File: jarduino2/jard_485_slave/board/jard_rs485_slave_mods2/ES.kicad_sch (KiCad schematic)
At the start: 29 parts, among them U1 BPC_Mod485

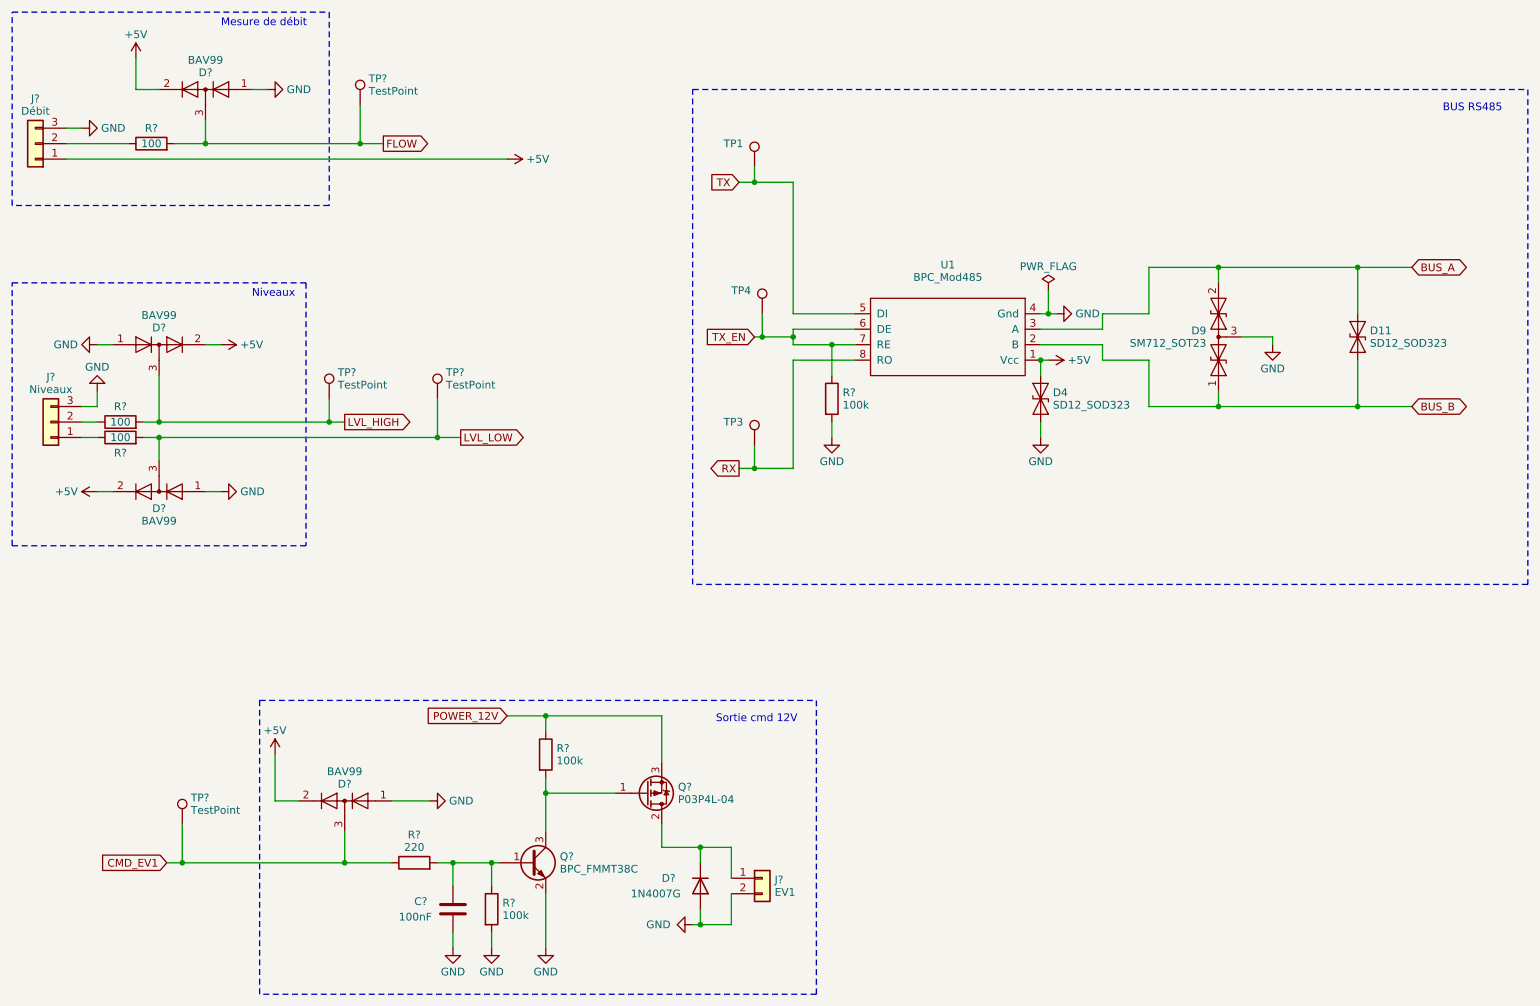
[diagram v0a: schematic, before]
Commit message: Suppression du module RS485 et remplacement par le CI MAX485E lui-même. Preparation version G...
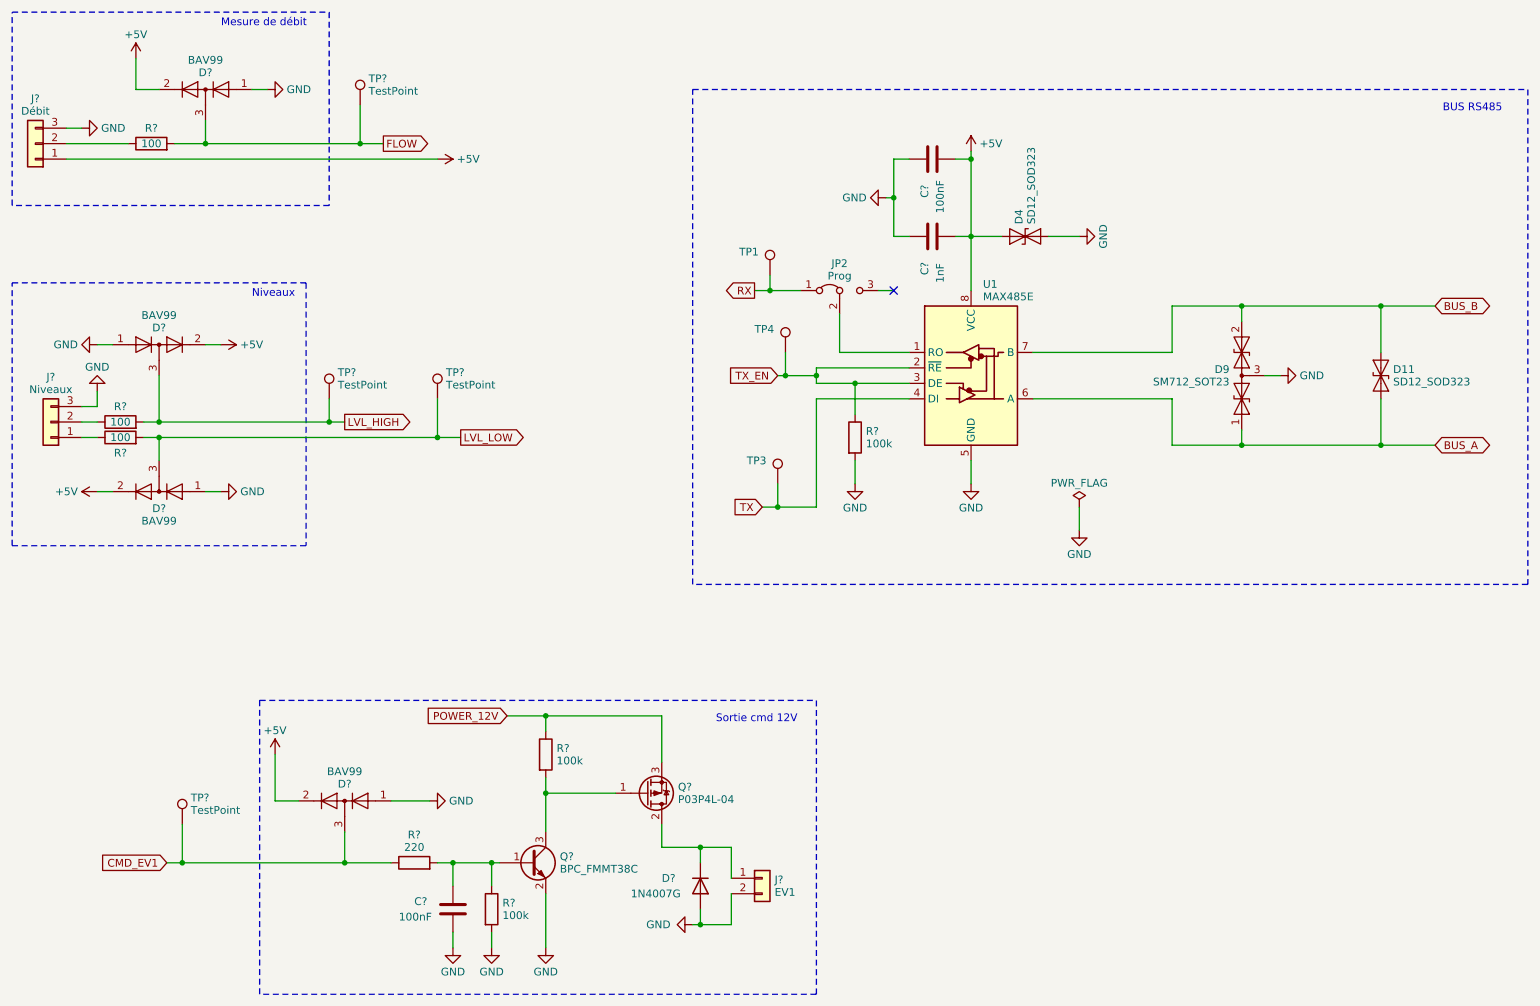
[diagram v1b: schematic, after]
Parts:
- removed U1: BPC_Mod485, bpc:BPC_Mod485, symbol bpc:BPC_Mod485
- added C?: 100nF, Capacitor_SMD:C_0603_1608Metric, symbol Device:C
- added C?: 1nF, Capacitor_SMD:C_0603_1608Metric, symbol Device:C
- added JP2: Prog, Connector_PinHeader_2.54mm:PinHeader_1x03_P2.54mm_Vertical, symbol Jumper:Jumper_3_Bridged12
- added U1: MAX485E, bpc:BPC_MAX485E_SOIC127P600X175-8N, symbol bpc:BPC_MAX485E
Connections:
- net +5V: now also C?.2, C?.2, U1.8 (VCC)
- net BUS_A: now also D11.1 (A1), D9.1 (A1), U1.6 (A); no longer D11.2 (A2), D9.2 (A2)
- net BUS_B: now also D11.2 (A2), D9.2 (A2), U1.7 (B); no longer D11.1 (A1), D9.1 (A1)
- net GND: now also C?.1, C?.1, U1.5 (GND)
- net RX: now also TP1.1, JP2.1 (A); no longer TP3.1
- net TX: now also TP3.1, U1.4 (DI); no longer TP1.1
- net TX_EN: now also U1.2 (~{RE}), U1.3 (DE)
- new net: JP2.2 (C), U1.1 (RO)
- no-connect marks 0 -> 1
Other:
- moved on the sheet: D11, D4, D9, R?, TP1, TP3, TP4

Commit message: Finitions avant production
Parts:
- added TP1 (x2): TestPoint, TestPoint:TestPoint_Pad_D1.5mm, symbol Connector:TestPoint
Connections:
- net BUS_A: now also TP1.1
- net BUS_B: now also TP1.1
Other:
- moved on the sheet: D11
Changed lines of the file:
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@@
   (junction (at 107.95 137.16) (diameter 0) (color 0 0 0 0)
   )
+  (junction (at 251.46 69.85) (diameter 0) (color 0 0 0 0)
+  )
   (junction (at 146.05 102.87) (diameter 0) (color 0 0 0 0)
+  )
+  (junction (at 251.46 92.71) (diameter 0) (color 0 0 0 0)
   )
   (junction (at 90.17 91.44) (diameter 0) (color 0 0 0 0)
@@
     (stroke (width 0) (type default))
   )
+  (wire (pts (xy 251.46 69.85) (xy 254 69.85))
+    (stroke (width 0) (type default))
+  )
   (wire (pts (xy 77.47 43.18) (xy 81.28 43.18))
     (stroke (width 0) (type default))
@@
     (stroke (width 0) (type default))
   )
-  (wire (pts (xy 245.11 85.09) (xy 245.11 92.71))
+  (wire (pts (xy 251.46 92.71) (xy 254 92.71))
+    (stroke (width 0) (type default))
+  )
+  (wire (pts (xy 245.11 83.82) (xy 245.11 92.71))
     (stroke (width 0) (type default))
   )
@@
     (stroke (width 0) (type default))
   )
-  (wire (pts (xy 245.11 92.71) (xy 254 92.71))
+  (wire (pts (xy 245.11 92.71) (xy 251.46 92.71))
     (stroke (width 0) (type default))
   )
@@
     (stroke (width 0) (type default))
   )
-  (wire (pts (xy 245.11 69.85) (xy 245.11 77.47))
+  (wire (pts (xy 245.11 69.85) (xy 245.11 76.2))
     (stroke (width 0) (type default))
   )
@@
     (stroke (width 0) (type default))
   )
+  (wire (pts (xy 251.46 68.58) (xy 251.46 69.85))
+    (stroke (width 0) (type default))
+  )
   (wire (pts (xy 74.93 156.21) (xy 74.93 161.29))
     (stroke (width 0) (type default))
@@
     (stroke (width 0) (type default))
   )
-  (wire (pts (xy 245.11 69.85) (xy 254 69.85))
+  (wire (pts (xy 245.11 69.85) (xy 251.46 69.85))
     (stroke (width 0) (type default))
   )
   (wire (pts (xy 34.29 88.9) (xy 31.75 88.9))
+    (stroke (width 0) (type default))
+  )
+  (wire (pts (xy 251.46 91.44) (xy 251.46 92.71))
     (stroke (width 0) (type default))
   )
@@
         (path "/5ae93d62-0543-4c0e-b37d-d67af6219e1b/dec80786-a2aa-49f2-be55-5994d7e13863"
           (reference "#PWR023") (unit 1)
+        )
+      )
+    )
+  )
+  (symbol (lib_id "Connector:TestPoint") (at 251.46 91.44 0) (unit 1)
+    (in_bom yes) (on_board yes) (dnp no)
+    (property "Reference" "TP1" (at 246.38 87.63 0)
+      (effects (font (size 1.27 1.27)) (justify left))
+    )
+    (property "Value" "TestPoint" (at 252.857 89.162 0)
+      (effects (font (size 1.27 1.27)) (justify left) hide)
+    )
+    (property "Footprint" "TestPoint:TestPoint_Pad_D1.5mm" (at 256.54 91.44 0)
+      (effects (font (size 1.27 1.27)) hide)
+    )
+    (property "Datasheet" "~" (at 256.54 91.44 0)
+      (effects (font (size 1.27 1.27)) hide)
+    )
+    (property "RefFabricant" "" (at 251.46 91.44 0)
+      (effects (font (size 1.27 1.27)) hide)
+    )
+    (property "RefFournisseur" "" (at 251.46 91.44 0)
+      (effects (font (size 1.27 1.27)) hide)
+    )
+    (property "Price" "0" (at 251.46 91.44 0)
+      (effects (font (size 1.27 1.27)) hide)
+    )
+    (pin "1")
+    (instances
+      (project "jard_rs485_slave_mods2"
+        (path "/5ae93d62-0543-4c0e-b37d-d67af6219e1b/36e9fbeb-2032-4e73-95af-53e316cf916d"
+          (reference "TP1") (unit 1)
+        )
+        (path "/5ae93d62-0543-4c0e-b37d-d67af6219e1b/dec80786-a2aa-49f2-be55-5994d7e13863"
+          (reference "TP7") (unit 1)
         )
       )
@@
     )
   )
+  (symbol (lib_id "Connector:TestPoint") (at 251.46 68.58 0) (unit 1)
+    (in_bom yes) (on_board yes) (dnp no)
+    (property "Reference" "TP1" (at 246.38 64.77 0)
+      (effects (font (size 1.27 1.27)) (justify left))
+    )
+    (property "Value" "TestPoint" (at 252.857 66.302 0)
+      (effects (font (size 1.27 1.27)) (justify left) hide)
+    )
+    (property "Footprint" "TestPoint:TestPoint_Pad_D1.5mm" (at 256.54 68.58 0)
+      (effects (font (size 1.27 1.27)) hide)
+    )
+    (property "Datasheet" "~" (at 256.54 68.58 0)
+      (effects (font (size 1.27 1.27)) hide)
+    )
+    (property "RefFabricant" "" (at 251.46 68.58 0)
+      (effects (font (size 1.27 1.27)) hide)
+    )
+    (property "RefFournisseur" "" (at 251.46 68.58 0)
+      (effects (font (size 1.27 1.27)) hide)
+    )
+    (property "Price" "0" (at 251.46 68.58 0)
+      (effects (font (size 1.27 1.27)) hide)
+    )
+    (pin "1")
+    (instances
+      (project "jard_rs485_slave_mods2"
+        (path "/5ae93d62-0543-4c0e-b37d-d67af6219e1b/36e9fbeb-2032-4e73-95af-53e316cf916d"
+          (reference "TP1") (unit 1)
+        )
+        (path "/5ae93d62-0543-4c0e-b37d-d67af6219e1b/dec80786-a2aa-49f2-be55-5994d7e13863"
+          (reference "TP6") (unit 1)
+        )
+      )
+    )
+  )
   (symbol (lib_id "power:GND") (at 31.75 40.64 90) (unit 1)
     (in_bom yes) (on_board yes) (dnp no) (fields_autoplaced)
@@
     )
   )
-  (symbol (lib_id "Diode:SD12_SOD323") (at 245.11 81.28 90) (unit 1)
-    (in_bom yes) (on_board yes) (dnp no) (fields_autoplaced)
-    (property "Reference" "D11" (at 247.1166 80.256 90)
+  (symbol (lib_id "Diode:SD12_SOD323") (at 245.11 80.01 90) (unit 1)
+    (in_bom yes) (on_board yes) (dnp no) (fields_autoplaced)
+    (property "Reference" "D11" (at 247.1166 78.986 90)
       (effects (font (size 1.27 1.27)) (justify right))
     )
-    (property "Value" "SD12_SOD323" (at 247.1166 82.304 90)
+    (property "Value" "SD12_SOD323" (at 247.1166 81.034 90)
       (effects (font (size 1.27 1.27)) (justify right))
     )
-    (property "Footprint" "Diode_SMD:D_SOD-323" (at 250.19 81.28 0)
-      (effects (font (size 1.27 1.27)) hide)
-    )
-    (property "Datasheet" "https://www.littelfuse.com/~/media/electronics/datasheets/tvs_diode_arrays/littelfuse_tvs_diode_array_sd_c_datasheet.pdf.pdf" (at 245.11 81.28 0)
-      (effects (font (size 1.27 1.27)) hide)
-    )
-    (property "RefFabricant" "SD12-7" (at 245.11 81.28 0)
-      (effects (font (size 1.27 1.27)) hide)
-    )
-    (property "RefFournisseur" "3945781RL" (at 245.11 81.28 0)
-      (effects (font (size 1.27 1.27)) hide)
-    )
-    (property "Fabricant" "DIODES INC" (at 245.11 81.28 0)
-      (effects (font (size 1.27 1.27)) hide)
-    )
-    (property "Fournisseur" "Farnell" (at 245.11 81.28 0)
-      (effects (font (size 1.27 1.27)) hide)
-    )
-    (property "Description" "Diodes TVS simples" (at 245.11 81.28 0)
-      (effects (font (size 1.27 1.27)) hide)
-    )
-    (property "Price" "0,1272" (at 245.11 81.28 0)
-      (effects (font (size 1.27 1.27)) hide)
-    )
+    (property "Footprint" "Diode_SMD:D_SOD-323" (at 250.19 80.01 0)
+      (effects (font (size 1.27 1.27)) hide)
+    )
+    (property "Datasheet" "https://www.littelfuse.com/~/media/electronics/datasheets/tvs_diode_arrays/littelfuse_tvs_diode_array_sd_c_datasheet.pdf.pdf" (at 245.11 80.01 0)
+      (effects (font (size 1.27 1.27)) hide)
+    )
+    (property "RefFabricant" "SD12-7" (at 245.11 80.01 0)
+      (effects (font (size 1.27 1.27)) hide)
+    )
+    (property "RefFournisseur" "3945781RL" (at 245.11 80.01 0)
+      (effects (font (size 1.27 1.27)) hide)
+    )
+    (property "Fabricant" "DIODES INC" (at 245.11 80.01 0)
+      (effects (font (size 1.27 1.27)) hide)
+    )
+    (property "Fournisseur" "Farnell" (at 245.11 80.01 0)
+      (effects (font (size 1.27 1.27)) hide)
+    )
+    (property "Description" "Diodes TVS simples" (at 245.11 80.01 0)
+      (effects (font (size 1.27 1.27)) hide)
+    )
+    (property "Price" "0,1272" (at 245.11 80.01 0)
+      (effects (font (size 1.27 1.27)) hide)
+    )

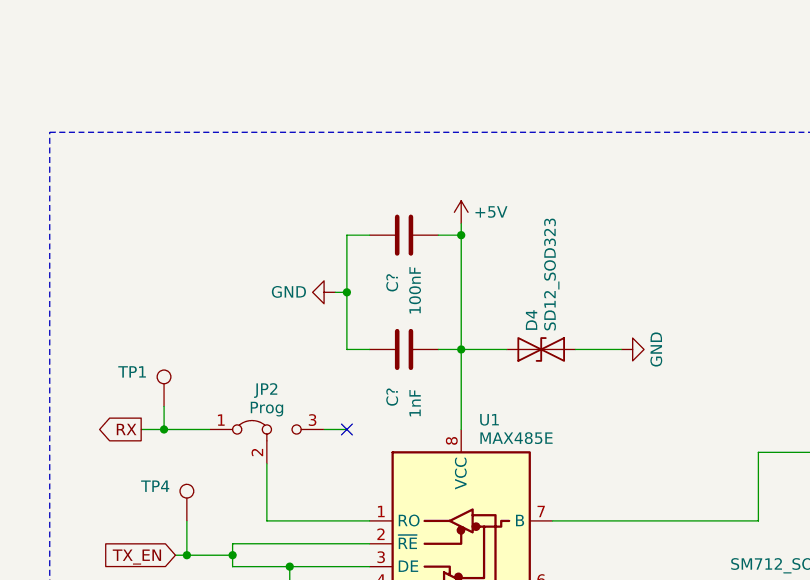
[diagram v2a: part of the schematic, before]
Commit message: Amélioration découplage RS485, MOS sur autre face
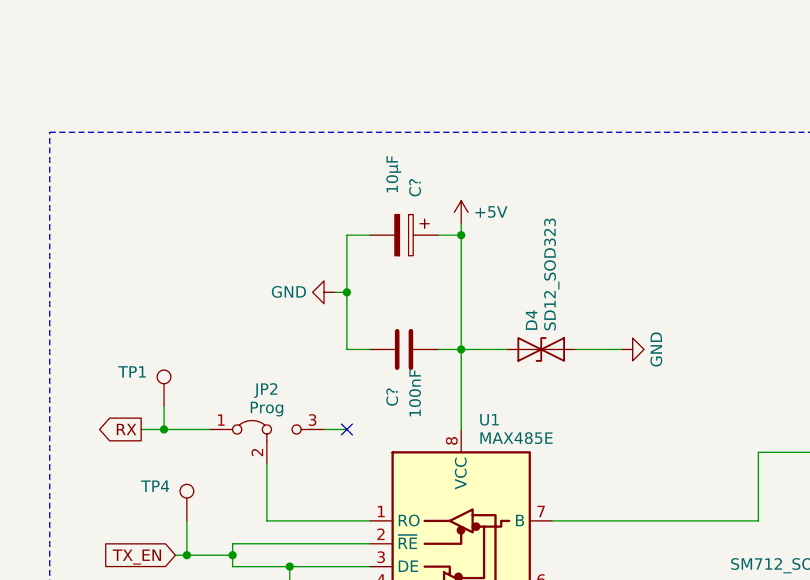
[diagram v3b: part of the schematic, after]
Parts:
- C?: value 100nF -> 10µF; footprint Capacitor_SMD:C_0603_1608Metric -> Capacitor_SMD:C_0805_2012Metric; symbol Device:C -> Device:C_Polarized
- C?: value 1nF -> 100nF
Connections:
- net +5V: now also C?.1; no longer C?.2
- net GND: now also C?.2; no longer C?.1
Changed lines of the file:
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@@
     (rev "G0")
     (company "BPC")
-    (comment 1 "Technologie avec modules Arduino Nano / Petite carte")
+    (comment 1 "Technologie avec module Arduino Nano / Petite carte")
     (comment 2 "Monitoring de tension d'alimentation")
     (comment 3 "1 sortie 12V/5A - 2 entrées TOR - 1 débimètre - 1 LED - Temp - RS485")
@@
     )
   )
-  (symbol (lib_id "Device:C") (at 171.45 45.72 90) (unit 1)
+  (symbol (lib_id "Device:C_Polarized") (at 171.45 45.72 270) (unit 1)
     (in_bom yes) (on_board yes) (dnp no)
-    (property "Reference" "C?" (at 170.18 52.07 0)
-      (effects (font (size 1.27 1.27)) (justify left))
-    )
-    (property "Value" "100nF" (at 172.72 54.61 0)
-      (effects (font (size 1.27 1.27)) (justify left))
-    )
-    (property "Footprint" "Capacitor_SMD:C_0603_1608Metric" (at 175.26 44.7548 0)
+    (property "Reference" "C?" (at 172.72 39.37 0)
+      (effects (font (size 1.27 1.27)) (justify left))
+    )
+    (property "Value" "10µF" (at 170.18 36.83 0)
+      (effects (font (size 1.27 1.27)) (justify left))
+    )
+    (property "Footprint" "Capacitor_SMD:C_0805_2012Metric" (at 167.64 46.6852 0)
       (effects (font (size 1.27 1.27)) hide)
     )
@@
       (effects (font (size 1.27 1.27)) (justify left))
     )
-    (property "Value" "1nF" (at 172.72 66.04 0)
-      (effects (font (size 1.27 1.27)) (justify left))
-    )
+    (property "Value" "100nF" (at 172.72 66.04 0)
+      (effects (font (size 1.27 1.27)) (justify left))
+    )

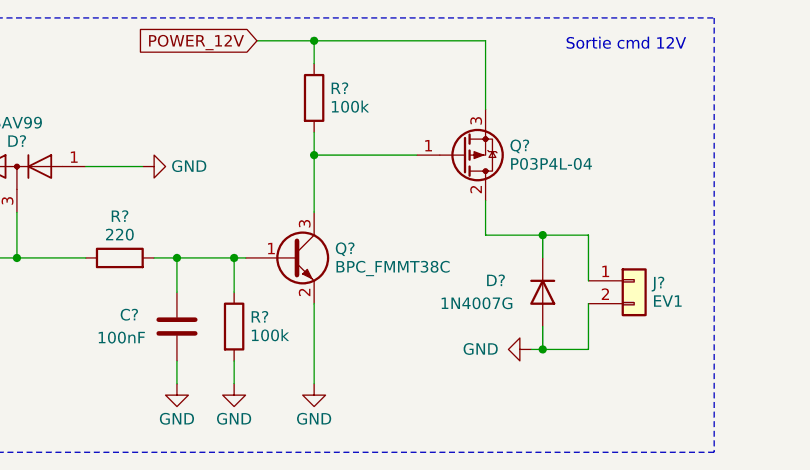
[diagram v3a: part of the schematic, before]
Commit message: Annotations sur le schéma (cond.603->805, Eq Transistor npn)
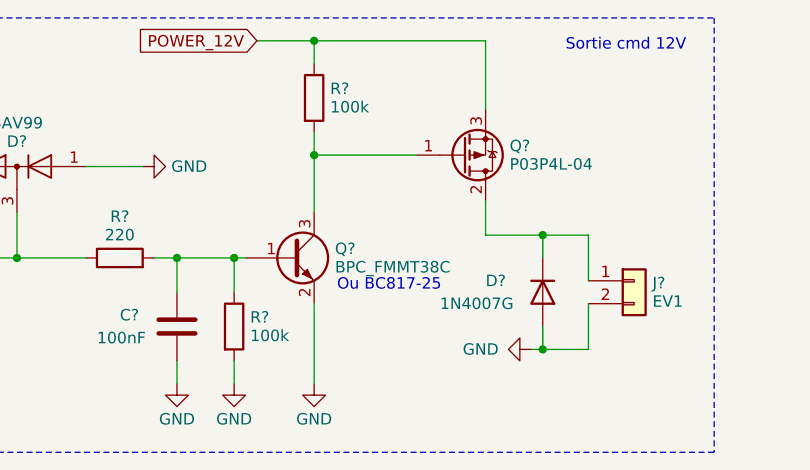
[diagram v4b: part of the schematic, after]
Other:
- note added: "Ou BC817-25"
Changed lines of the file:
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@@
+    (effects (font (size 1.27 1.27)) (justify left bottom))
+  )
+  (text "Ou BC817-25" (at 110.49 165.1 0)
     (effects (font (size 1.27 1.27)) (justify left bottom))
   )
